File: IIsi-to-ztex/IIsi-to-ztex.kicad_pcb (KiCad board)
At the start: 4 copper layers, 118 x 100 mm, 62 parts, among them J1 Conn_02x07_Odd_Even, J2 650906-5, J3 10029449-111RLF (HDMI A), J4 A2541HWR-2x6P (Pmod 2x6 F R), U1 SN74CB3T3245PWR, U10 SN74CB3T3245PWR, U11 SN74CB3T3245PWR, U12 TPD12S016PWR, U13 SN74CB3T3245PWR, U14 SN74LV1T125DCKR, U2 SN74CB3T3245PWR, U3 SN74CB3T3245PWR, U4 SN74CB3T3245PWR, U5 SN74CB3T3245PWR, U6 SN74CB3T3245PWR, U7 SN74CB3T3245PWR, U8 SN74CB3T3245PWR, U9 SN74CB3T3245PWR

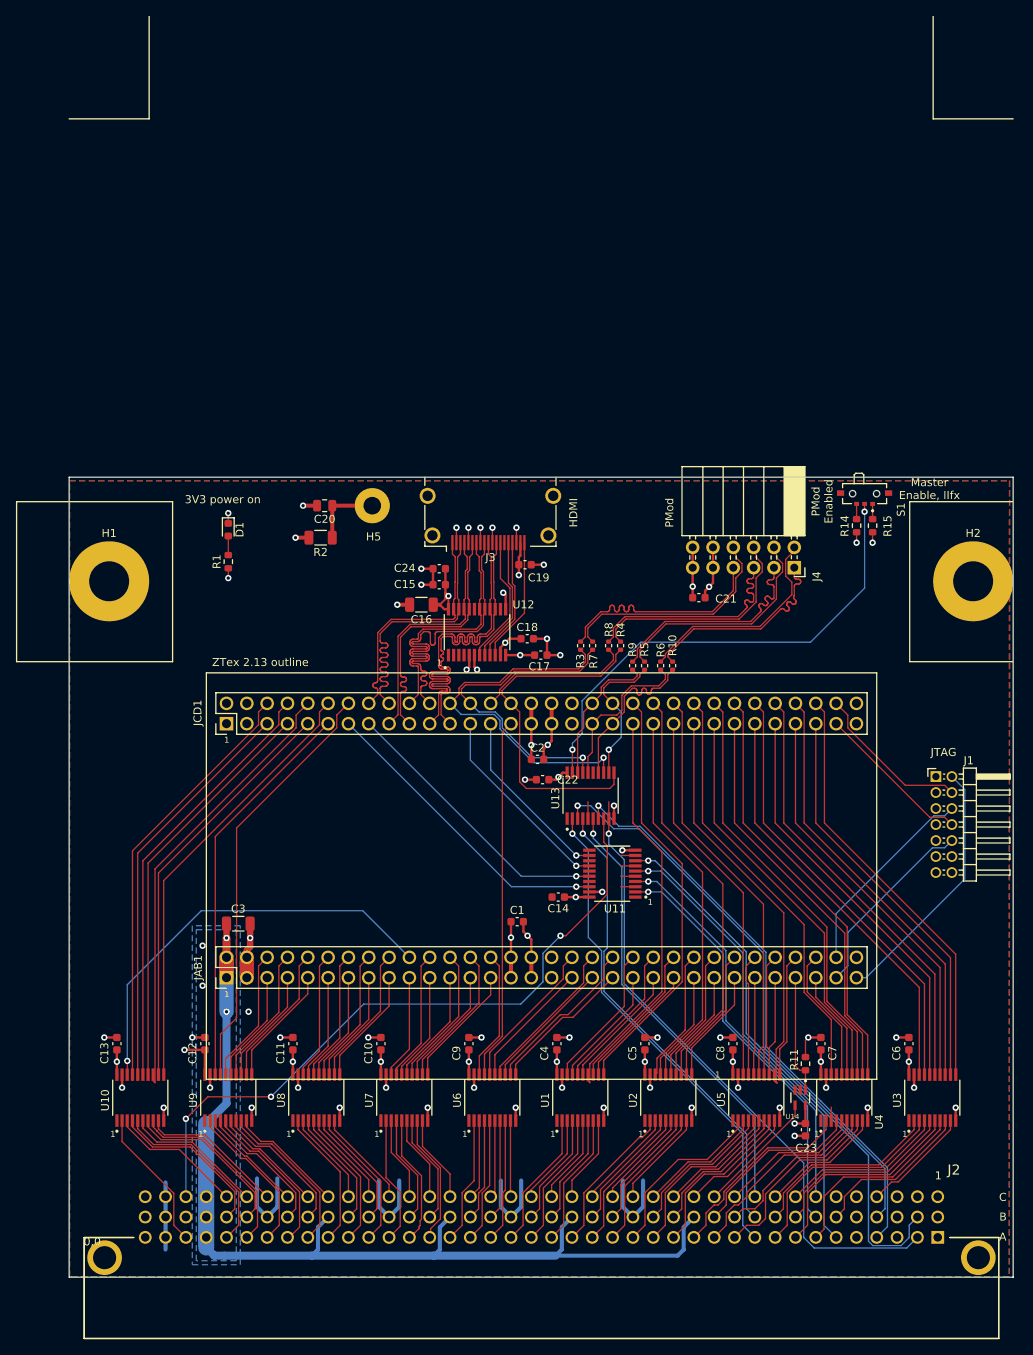
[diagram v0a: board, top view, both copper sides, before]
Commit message: 3V3 SRAM draft
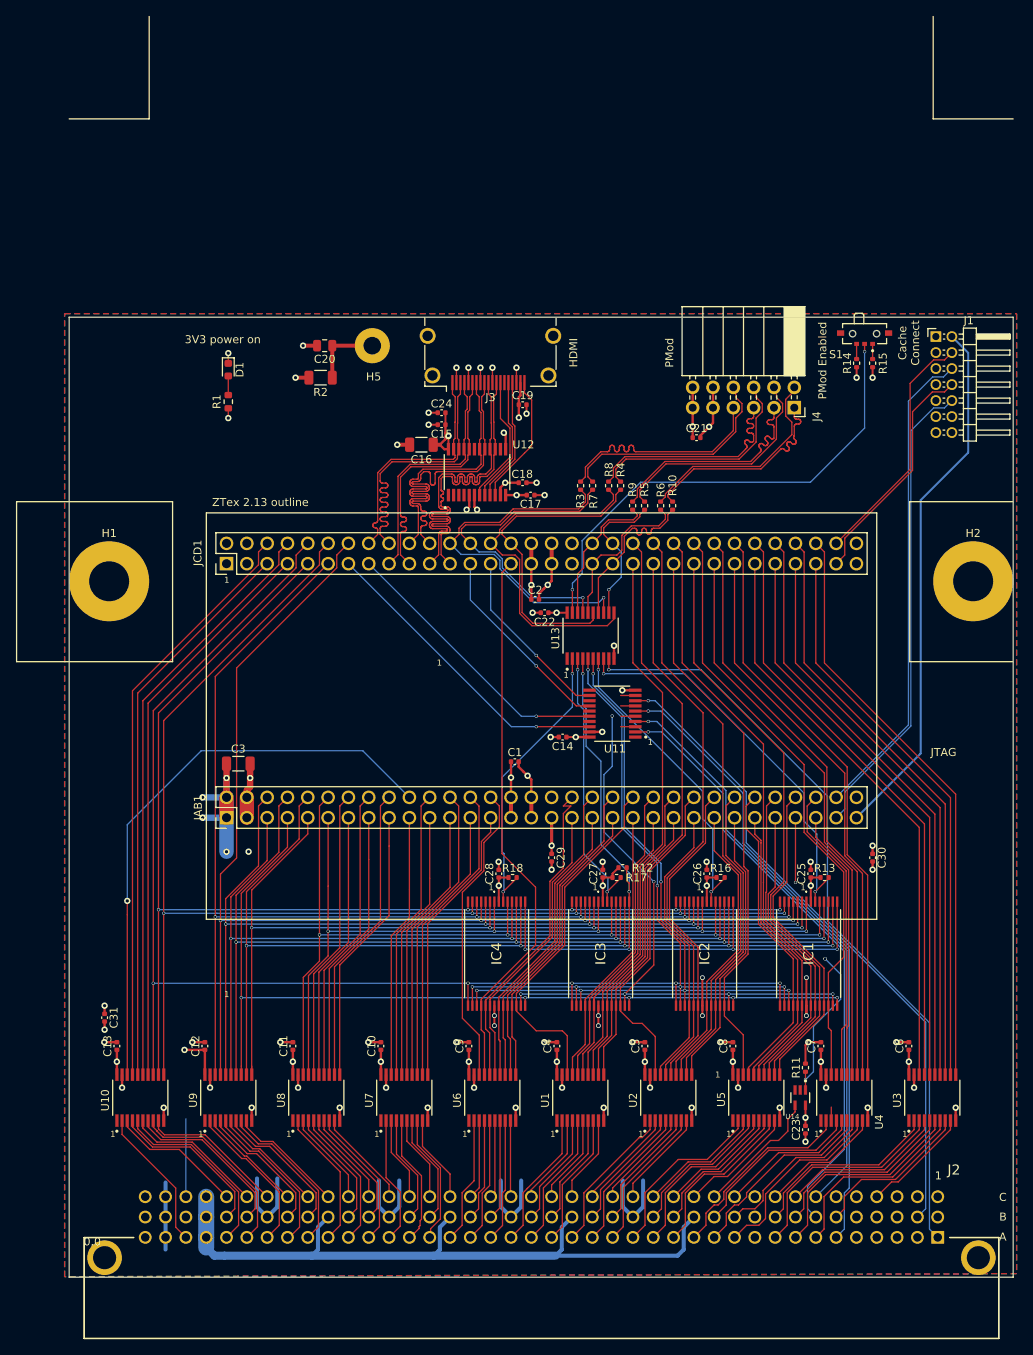
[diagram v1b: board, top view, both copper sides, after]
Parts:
- added C25: 100nF, Capacitor_SMD:C_0402_1005Metric, F.Cu at (188.3, 102.0)
- added C26: 100nF, Capacitor_SMD:C_0402_1005Metric, F.Cu at (175.3, 102.0)
- added C27: 100nF, Capacitor_SMD:C_0402_1005Metric, F.Cu at (162.3, 102.0)
- added C28: 100nF, Capacitor_SMD:C_0402_1005Metric, F.Cu at (149.3, 102.0)
- added C29: 1uF, Capacitor_SMD:C_0402_1005Metric, F.Cu at (155.9, 100.0)
- added C30: 1uF, Capacitor_SMD:C_0402_1005Metric, F.Cu at (196.0, 100.0)
- added C31: 1uF, Capacitor_SMD:C_0402_1005Metric, F.Cu at (100.0, 120.0)
- added IC1: IS61LV256AL-10TLI, For_SeeedStudio:IS61LV256AL10TLI, F.Cu at (188.0, 112.0)
- added IC2: IS61LV256AL-10TLI, For_SeeedStudio:IS61LV256AL10TLI, F.Cu at (175.0, 112.0)
- added IC3: IS61LV256AL-10TLI, For_SeeedStudio:IS61LV256AL10TLI, F.Cu at (162.0, 112.0)
- added IC4: IS61LV256AL-10TLI, For_SeeedStudio:IS61LV256AL10TLI, F.Cu at (149.0, 112.0)
- added R12: 10k, Resistor_SMD:R_0402_1005Metric, F.Cu at (164.8, 101.2)
- added R13: 10k, Resistor_SMD:R_0402_1005Metric, F.Cu at (190.0, 102.5)
- added R16: 10k, Resistor_SMD:R_0402_1005Metric, F.Cu at (177.0, 102.5)
- added R17: 10k, Resistor_SMD:R_0402_1005Metric, F.Cu at (164.0, 102.5)
- added R18: 10k, Resistor_SMD:R_0402_1005Metric, F.Cu at (151.0, 102.5)
- C1, C10, C11, C12, C13, C14, C15, C17, C18, C19, C2, C21, C22, C23, C24, C4, C5, C6, C7, C8, C9: footprint Capacitor_SMD:C_0603_1608Metric -> Capacitor_SMD:C_0402_1005Metric
- C3: value 47uF 10V+ -> 47uF 10V 1206
- R11, R14, R15: footprint Resistor_SMD:R_0603_1608Metric -> Resistor_SMD:R_0402_1005Metric
- moved J1 55.0 mm to (203.9, 34.9)
- moved C22 20.9 mm to (155.0, 69.4)
- moved R14 20.3 mm to (194.0, 38.2)
- moved R15 20.3 mm to (196.0, 38.2)
- moved C17 20.0 mm to (153.2, 54.7)
- moved C14 20.0 mm to (157.2, 84.9)
- moved C1 20.0 mm to (151.3, 88.0)
- moved C19 20.0 mm to (152.3, 43.4)
- moved C2 20.0 mm to (153.8, 67.7)
- moved C21 20.0 mm to (174.0, 47.5)
- moved C15 20.0 mm to (142.1, 45.9)
- moved C20 20.0 mm to (127.5, 36.0)
- moved C3 20.0 mm to (116.7, 88.2)
- moved D1 20.0 mm to (115.5, 39.0)
- moved H5 20.0 mm to (133.5, 36.0)
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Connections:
- net C16M_3V3 renamed PMOD-910-
- net ~MASTER_OE renamed CACHE_~CE
- U13 pad 11: PMOD-78- -> PMOD-78+
- U13 pad 15: Net-(U13-Pad15) -> PMOD-78-
- U13 pad 2: ~BGACK -> SRAM_B3_~WE
- U13 pad 3: ~IRQ2 -> SRAM_B2_~WE
- U13 pad 4: ~BG -> SRAM_~OE
- U13 pad 5: GND -> SRAM_A3
- U13 pad 6: ~BR -> SRAM_A2
- U13 pad 7: ~IRQ3 -> SRAM_B1_~WE
- U13 pad 8: C16M -> SRAM_B0_~WE
- U13 pad 9: ~FPU -> ~RBV
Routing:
- net A13_3V3: track 17.8 -> 133.1 mm, vias 0 -> 5
- net A11_3V3: track 17.3 -> 131.6 mm, vias 0 -> 5
- net A10_3V3: track 14.0 -> 126.5 mm, vias 0 -> 5
- net A4_3V3: track 56.4 -> 164.0 mm, vias 0 -> 5
- net A6_3V3: track 54.9 -> 158.3 mm, vias 0 -> 5
- net A14_3V3: track 15.0 -> 117.9 mm, vias 0 -> 5
- net A9_3V3: track 16.8 -> 119.5 mm, vias 0 -> 5
- net CACHE_~CE: track 61.2 -> 163.1 mm, vias 2 -> 8
- net A5_3V3: track 51.6 -> 153.3 mm, vias 0 -> 5
- net A8_3V3: track 53.0 -> 154.0 mm, vias 0 -> 5
- net A7_3V3: track 49.7 -> 149.0 mm, vias 0 -> 5
- net A15_3V3: track 16.0 -> 115.1 mm, vias 0 -> 5
- net SRAM_~OE: track 0.00 -> 98.7 mm, vias 0 -> 6
- net A12_3V3: track 14.5 -> 113.0 mm, vias 0 -> 5
- net ~RBV: track 0.00 -> 96.1 mm, vias 0 -> 1
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- removed copper zone on B.Cu, net +5V
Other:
- board size 118 x 100 mm -> 118 x 120 mm
- net class Default: via_dia 0.8 -> 0.4; via_drill 0.4 -> 0.3
- net class PWR added: clearance 0.17, trace_width 0.25, via_dia 0.8, via_drill 0.4
- rule via_min_size: 0.45 -> 0.4
- board text added: "Cache Connect"
- board text removed: "Master Enable, IIfx"
